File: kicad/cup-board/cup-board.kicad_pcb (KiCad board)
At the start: 4 copper layers, 68 x 68 mm, 102 parts, among them J2 EARCUP_SPKR, J7 CUP_IN (A2B + panel audio, ma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, J8 CUP_OUT (A2B to next cup), Q1 AO3401A, Q2 MMBT3904, U1 ADAU1861, U2 LSM6DSV16BX, U3 MAXM86161, U4 AQW612S, U5 AQW612S, U6 AD2428WBCPZ (sub-node), U7 TPS62161DSG (1V8), U8 ADP7118AUJZ-3.3-R7 (3V3_MIC), U9 ADP7118AUJZ-3.3-R7 (VLED)

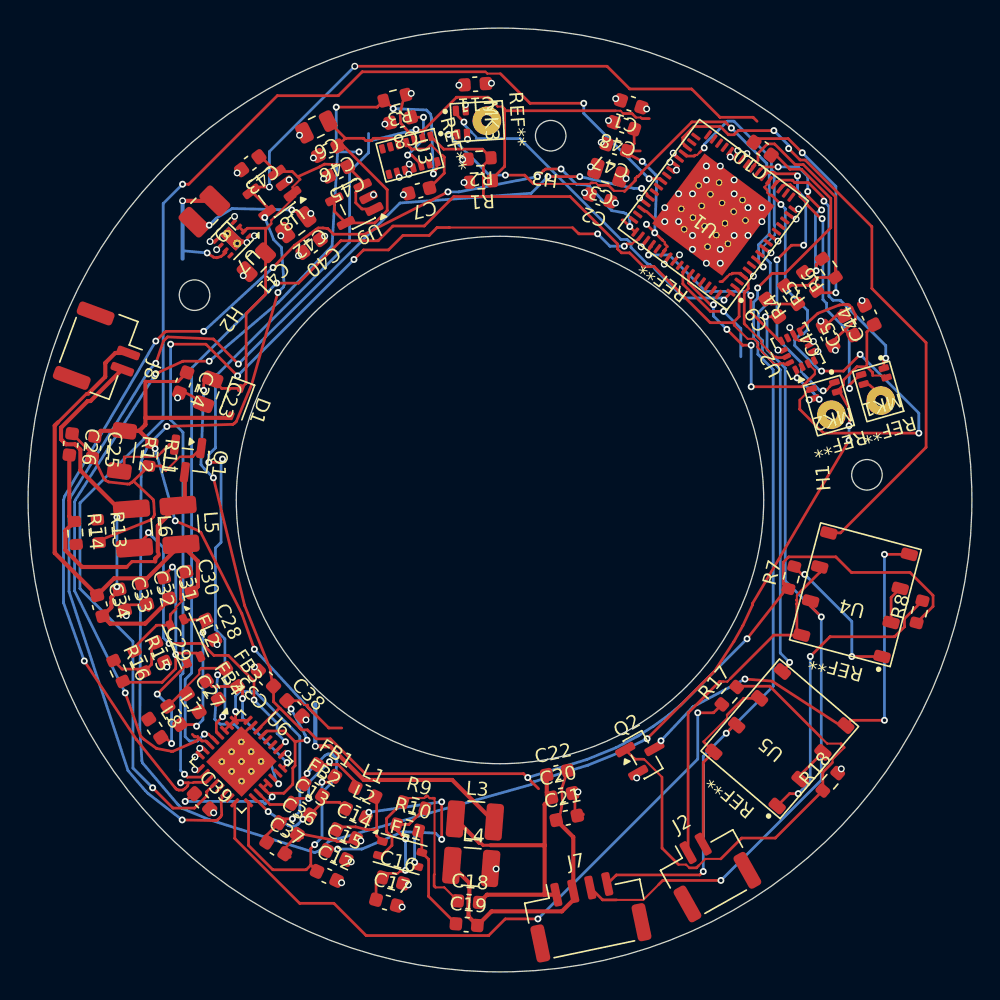
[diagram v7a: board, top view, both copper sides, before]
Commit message: [LIMA] cup PCB: U6 turned +90 (B pins face the B chain), decaps re-seated end-on; autorouted (WIP)
Co-Authored-By: Claude Opus 5.5 <noreply@anthropic.com>
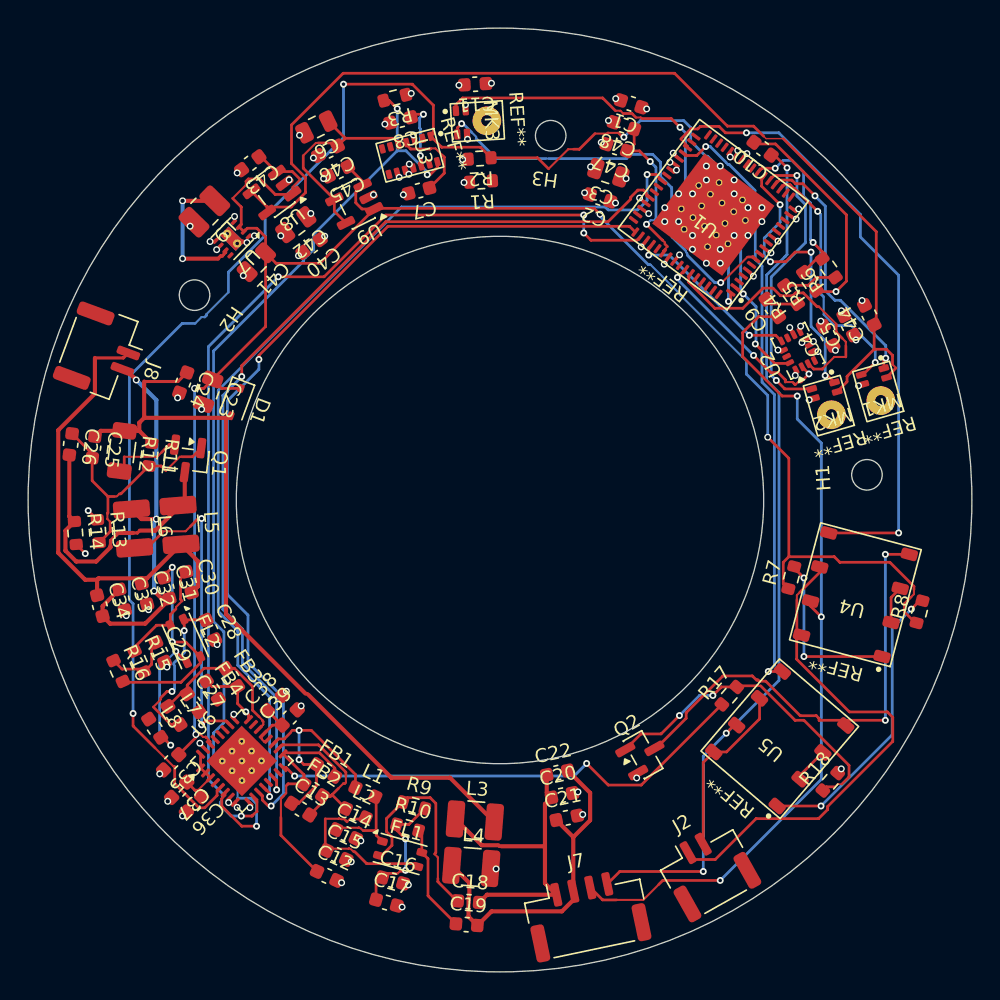
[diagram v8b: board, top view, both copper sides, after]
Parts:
- moved C35 9.11 mm to (126.3, 118.9), turned to -134.7 degrees
- moved C39 8.74 mm to (134.8, 115.7), turned to 45.3 degrees
- moved C37 8.12 mm to (126.9, 120.9), turned to -134.7 degrees
- moved C36 7.01 mm to (128.0, 121.9), turned to -134.7 degrees
- moved C38 1.46 mm to (133.8, 114.6), turned to 45.3 degrees
- moved U6 0.05 mm to (131.4, 118.8), turned to 45.3 degrees
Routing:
- net /3V3_MIC: track 169.2 -> 75.1 mm, vias 8 -> 0
- net /SCL: track 88.2 -> 0.00 mm, vias 4 -> 0
- net /I2S0_SDATAI: track 96.4 -> 71.6 mm, vias 4 -> 2
- net /SDA: track 94.1 -> 116.6 mm, vias 2 -> 5
- net /A2B_VOUT2: track 25.1 -> 4.13 mm, vias 4 -> 0
- net Net-(MK2-OUT-): track 38.5 -> 21.2 mm, vias 4 -> 2
- net /1V8: track 27.7 -> 11.6 mm, vias 25 -> 27
- net /VIN_CUP: track 120.7 -> 136.7 mm
- net /I2S0_SDATAO: track 84.5 -> 68.8 mm, vias 6 -> 2
- net /ADC2_P: track 18.4 -> 3.90 mm
- net /K2_CTL: track 49.4 -> 35.3 mm
- net /A2B_VOUT1: track 18.9 -> 4.89 mm, vias 2 -> 0
- net /I2S0_FSYNC: track 81.8 -> 68.1 mm, vias 9 -> 2
- net /K2_B: track 36.4 -> 23.5 mm, vias 0 -> 2
- net /SPKR_1: track 26.3 -> 36.6 mm
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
